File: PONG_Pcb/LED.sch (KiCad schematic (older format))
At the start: 4 parts, among them J1 LED_Display_Conn, U1 PC817

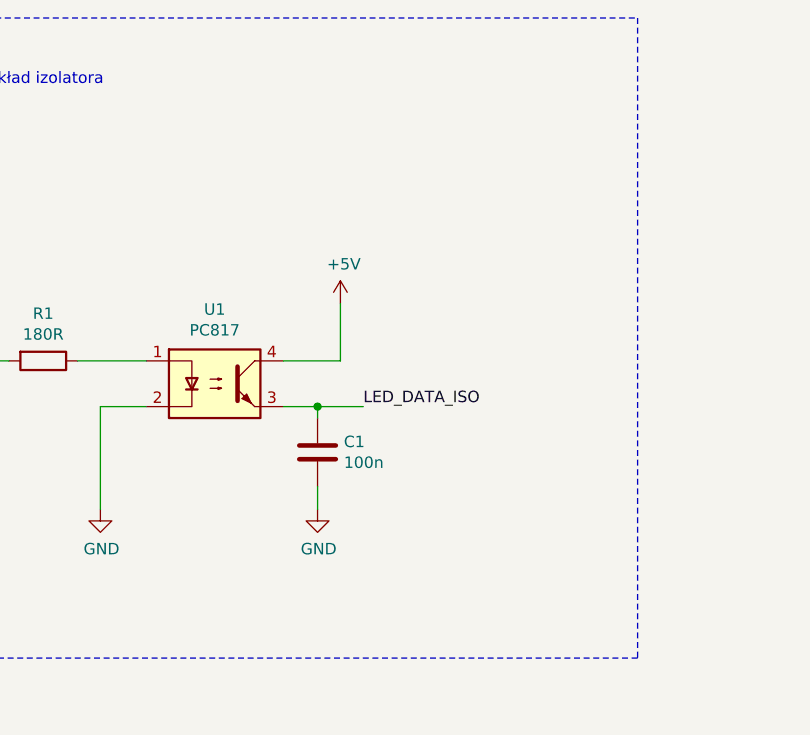
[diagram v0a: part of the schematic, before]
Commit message: Poprawki layoutu
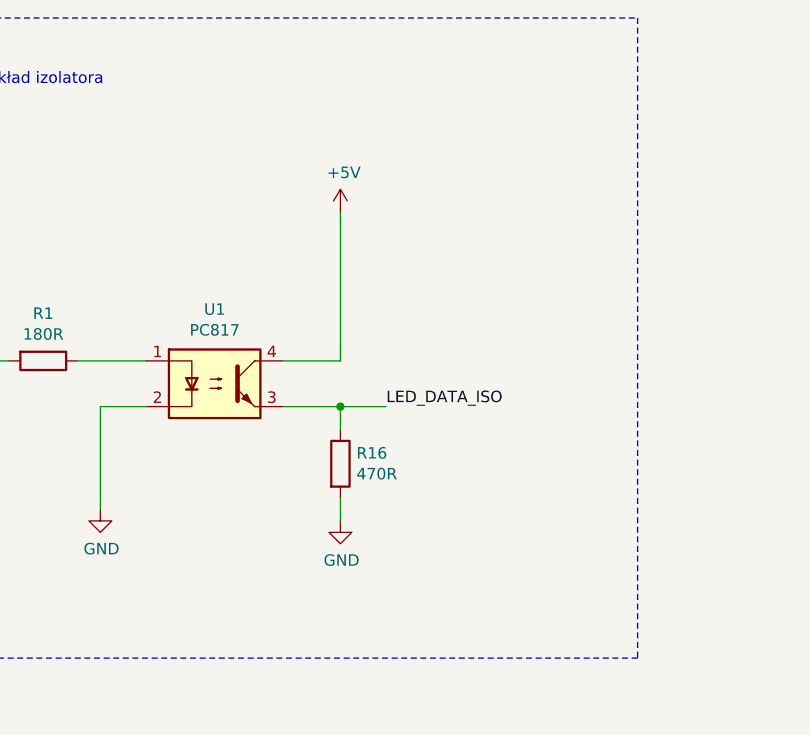
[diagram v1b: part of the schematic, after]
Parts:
- removed C1: 100n, Capacitor_SMD:C_0603_1608Metric_Pad1.05x0.95mm_HandSolder, symbol Device:C
- added R16: 470R, Resistor_SMD:R_0603_1608Metric_Pad1.05x0.95mm_HandSolder, symbol Device:R
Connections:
- net GND: now also R16.2
- net LED_DATA_ISO: now also R16.1
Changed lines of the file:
@@
 Wire Wire Line
 	3250 2550 3500 2550
-Wire Wire Line
-	3500 2550 3500 2300
-Wire Wire Line
-	3250 2750 3400 2750
 Wire Notes Line
 	1150 1050 4800 1050
@@
 Text Notes 1950 1350 0    50   ~ 0
 Układ izolatora
-$Comp
-L Device:C C1
-U 1 1 5E90693A
-P 3400 2950
-F 0 "C1" H 3515 2996 50  0000 L CNN
-F 1 "100n" H 3515 2905 50  0000 L CNN
-F 2 "Capacitor_SMD:C_0603_1608Metric_Pad1.05x0.95mm_HandSolder" H 3438 2800 50  0001 C CNN
-F 3 "~" H 3400 2950 50  0001 C CNN
-	1    3400 2950
-	1    0    0    -1
-$EndComp
-$Comp
-L power:GND #PWR02
-U 1 1 5E906F7A
-P 3400 3200
-F 0 "#PWR02" H 3400 2950 50  0001 C CNN
-F 1 "GND" H 3405 3027 50  0000 C CNN
-F 2 "" H 3400 3200 50  0001 C CNN
-F 3 "" H 3400 3200 50  0001 C CNN
-	1    3400 3200
-	1    0    0    -1
-$EndComp
-Wire Wire Line
-	3400 2750 3400 2800
-Connection ~ 3400 2750
-Wire Wire Line
-	3400 2750 3600 2750
-Wire Wire Line
-	3400 3100 3400 3200
 Text HLabel 1900 2550 0    50   Input ~ 0
 LED_DATA
-Text Label 3600 2750 0    50   ~ 0
+Text Label 3700 2750 0    50   ~ 0
 LED_DATA_ISO
 Text Label 7950 2800 0    50   ~ 0
@@
 L power:+5V #PWR?
 U 1 1 5EA0B611
-P 3500 2300
+P 3500 1900
 AR Path="/5E80B14C/5EA0B611" Ref="#PWR?"  Part="1"
 AR Path="/5E80C133/5EA0B611" Ref="#PWR03"  Part="1"
-F 0 "#PWR03" H 3500 2150 50  0001 C CNN
-F 1 "+5V" H 3515 2473 50  0000 C CNN
-F 2 "" H 3500 2300 50  0001 C CNN
-F 3 "" H 3500 2300 50  0001 C CNN
-	1    3500 2300
+F 0 "#PWR03" H 3500 1750 50  0001 C CNN
+F 1 "+5V" H 3515 2073 50  0000 C CNN
+F 2 "" H 3500 1900 50  0001 C CNN
+F 3 "" H 3500 1900 50  0001 C CNN
+	1    3500 1900
 	1    0    0    -1
 $EndComp
@@
 	1    0    0    -1
 $EndComp
+$Comp
+L Device:R R16
+U 1 1 5EC2CC66
+P 3500 3000
+F 0 "R16" H 3570 3046 50  0000 L CNN
+F 1 "470R" H 3570 2955 50  0000 L CNN
+F 2 "Resistor_SMD:R_0603_1608Metric_Pad1.05x0.95mm_HandSolder" V 3430 3000 50  0001 C CNN
+F 3 "~" H 3500 3000 50  0001 C CNN
+	1    3500 3000
+	1    0    0    -1
+$EndComp
+$Comp
+L power:GND #PWR02
+U 1 1 5EC2E6B4
+P 3500 3250
+F 0 "#PWR02" H 3500 3000 50  0001 C CNN
+F 1 "GND" H 3505 3077 50  0000 C CNN
+F 2 "" H 3500 3250 50  0001 C CNN
+F 3 "" H 3500 3250 50  0001 C CNN
+	1    3500 3250
+	1    0    0    -1
+$EndComp
+Wire Wire Line
+	3250 2750 3500 2750
+Wire Wire Line
+	3500 1900 3500 2550
+Connection ~ 3500 2750
+Wire Wire Line
+	3500 2750 3700 2750
+Wire Wire Line
+	3500 2750 3500 2850
+Wire Wire Line
+	3500 3250 3500 3150
 $EndSCHEMATC

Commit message: Poprawki
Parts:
- added C1: 100n, Capacitor_SMD:C_0603_1608Metric_Pad1.05x0.95mm_HandSolder, symbol Device:C
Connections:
- net GND: now also C1.2; no longer R16.2
- net LED_DATA_ISO: now also R16.2; no longer R16.1, U1.3
- new net: C1.1, R16.1, U1.3
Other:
- moved on the sheet: R16
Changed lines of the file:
@@
 Text HLabel 1900 2550 0    50   Input ~ 0
 LED_DATA
-Text Label 3700 2750 0    50   ~ 0
+Text Label 4250 2750 0    50   ~ 0
 LED_DATA_ISO
 Text Label 7950 2800 0    50   ~ 0
@@
 	1    0    0    -1
 $EndComp
+Wire Wire Line
+	3500 1900 3500 2550
+Wire Wire Line
+	4050 2750 4250 2750
 $Comp
 L Device:R R16
 U 1 1 5EC2CC66
+P 3900 2750
+F 0 "R16" V 4100 2700 50  0000 L CNN
+F 1 "470R" V 4000 2650 50  0000 L CNN
+F 2 "Resistor_SMD:R_0603_1608Metric_Pad1.05x0.95mm_HandSolder" V 3830 2750 50  0001 C CNN
+F 3 "~" H 3900 2750 50  0001 C CNN
+	1    3900 2750
+	0    -1   -1   0
+$EndComp
+Connection ~ 3500 2750
+Wire Wire Line
+	3500 2750 3750 2750
+Wire Wire Line
+	3250 2750 3500 2750
+$Comp
+L Device:C C1
+U 1 1 5EC2D8FC
 P 3500 3000
-F 0 "R16" H 3570 3046 50  0000 L CNN
-F 1 "470R" H 3570 2955 50  0000 L CNN
-F 2 "Resistor_SMD:R_0603_1608Metric_Pad1.05x0.95mm_HandSolder" V 3430 3000 50  0001 C CNN
+F 0 "C1" H 3615 3046 50  0000 L CNN
+F 1 "100n" H 3615 2955 50  0000 L CNN
+F 2 "Capacitor_SMD:C_0603_1608Metric_Pad1.05x0.95mm_HandSolder" H 3538 2850 50  0001 C CNN
 F 3 "~" H 3500 3000 50  0001 C CNN
 	1    3500 3000
@@
 $EndComp
 $Comp
-L power:GND #PWR02
-U 1 1 5EC2E6B4
+L power:GND #PWR0114
+U 1 1 5EC2E350
 P 3500 3250
-F 0 "#PWR02" H 3500 3000 50  0001 C CNN
+F 0 "#PWR0114" H 3500 3000 50  0001 C CNN
 F 1 "GND" H 3505 3077 50  0000 C CNN
 F 2 "" H 3500 3250 50  0001 C CNN
@@
 $EndComp
 Wire Wire Line
-	3250 2750 3500 2750
+	3500 3150 3500 3250
 Wire Wire Line
-	3500 1900 3500 2550
-Connection ~ 3500 2750
-Wire Wire Line
-	3500 2750 3700 2750
-Wire Wire Line
-	3500 2750 3500 2850
-Wire Wire Line
-	3500 3250 3500 3150
+	3500 2850 3500 2750
 $EndSCHEMATC
